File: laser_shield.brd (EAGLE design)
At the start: 114 x 85.1 mm, 18 parts, among them IC1 74AC08N, U1 ARDUINO_SHIELDLONGPADS

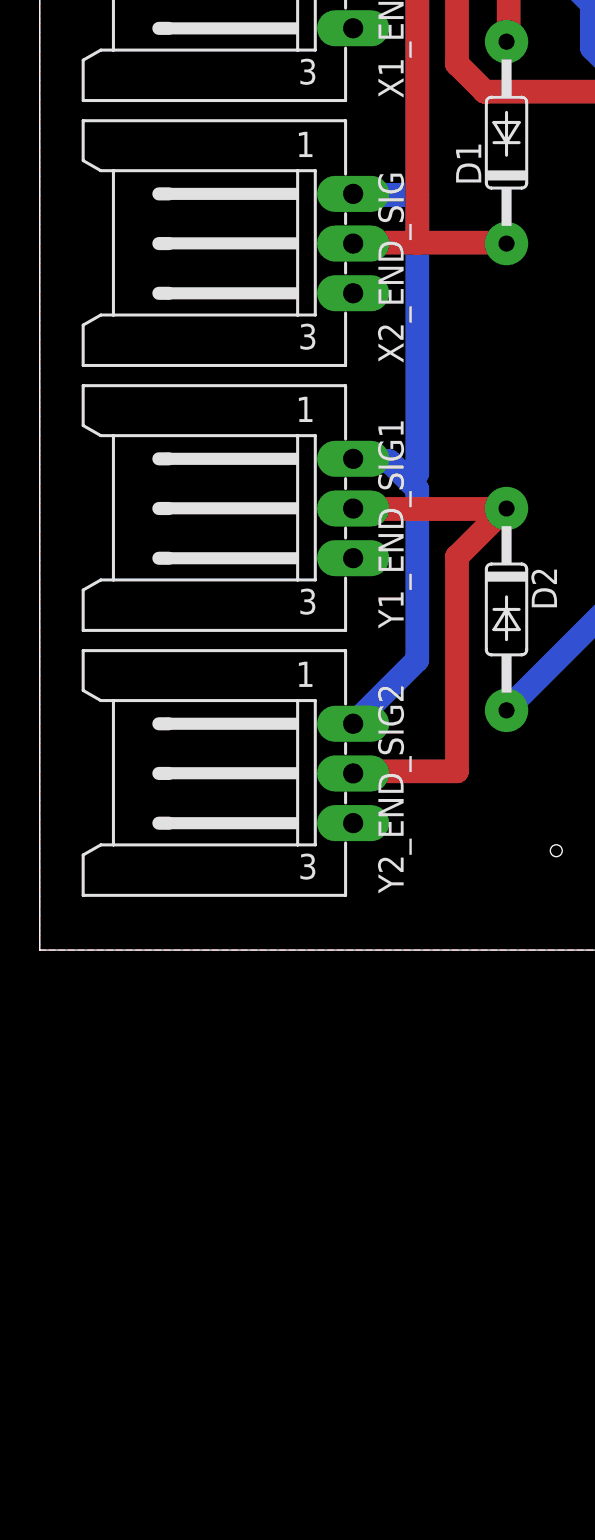
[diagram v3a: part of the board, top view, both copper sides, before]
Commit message: Added Z_LIMIT
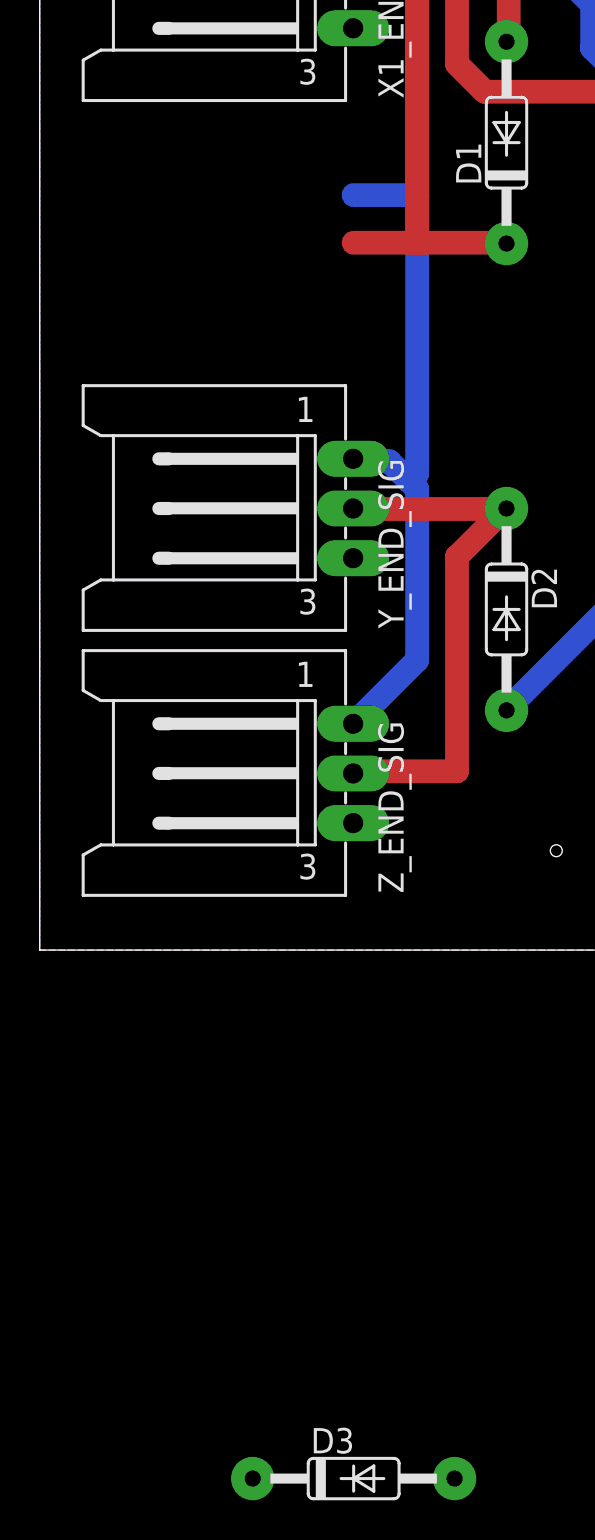
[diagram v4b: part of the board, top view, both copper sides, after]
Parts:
- removed X2_END_SIG: (no value), con-amp-mt:L03P
- added D3: 1N4148DO35-10, diode:DO35-10
- renumbered Y1_END_SIG1 to Y_END_SIG, Y2_END_SIG2 to Z_END_SIG
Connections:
- new net Z_END_STOP: D3.C, Z_END_SIG.2
- net GND: no longer X2_END_SIG.3
- net LIMIT_Z: now also D3.A
- net VCC_24: no longer X2_END_SIG.1
- net X_END_STOP: no longer X2_END_SIG.2
- net Y_END_STOP: no longer Z_END_SIG.2
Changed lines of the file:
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@@
 <attribute name="MF" value="" x="9.525" y="60.96" size="1.778" layer="27" rot="R90" display="off"/>
-</element>
-<element name="X2_END_SIG" library="con-amp-mt" package="L03P" value="" x="9.525" y="35.56" rot="R90">
-<attribute name="MPN" value="" x="9.525" y="35.56" size="1.778" layer="27" rot="R90" display="off"/>
-<attribute name="OC_NEWARK" value="unknown" x="9.525" y="35.56" size="1.778" layer="27" rot="R90" display="off"/>
-<attribute name="OC_FARNELL" value="unknown" x="9.525" y="35.56" size="1.778" layer="27" rot="R90" display="off"/>
-<attribute name="MF" value="" x="9.525" y="35.56" size="1.778" layer="27" rot="R90" display="off"/>
 </element>
 <element name="X1_END_SIG" library="con-amp-mt" package="L03P" value="" x="9.525" y="48.895" rot="R90">
@@
 <attribute name="MF" value="" x="127.635" y="29.21" size="1.778" layer="27" rot="R270" display="off"/>
 </element>
-<element name="Y1_END_SIG1" library="con-amp-mt" package="L03P" value="" x="9.525" y="22.225" rot="R90">
+<element name="Y_END_SIG" library="con-amp-mt" package="L03P" value="" x="9.525" y="22.225" rot="R90">
 <attribute name="MPN" value="" x="-12.065" y="1.27" size="1.778" layer="27" rot="R90" display="off"/>
 <attribute name="OC_NEWARK" value="unknown" x="-12.065" y="1.27" size="1.778" layer="27" rot="R90" display="off"/>
@@
 <attribute name="MF" value="" x="-12.065" y="1.27" size="1.778" layer="27" rot="R90" display="off"/>
 </element>
-<element name="Y2_END_SIG2" library="con-amp-mt" package="L03P" value="" x="9.525" y="8.89" rot="R90">
+<element name="Z_END_SIG" library="con-amp-mt" package="L03P" value="" x="9.525" y="8.89" rot="R90">
 <attribute name="MPN" value="" x="-12.065" y="-12.065" size="1.778" layer="27" rot="R90" display="off"/>
 <attribute name="OC_NEWARK" value="unknown" x="-12.065" y="-12.065" size="1.778" layer="27" rot="R90" display="off"/>
@@
 <attribute name="MF" value="" x="18.415" y="97.79" size="1.778" layer="27" display="off"/>
 </element>
+<element name="D3" library="diode" package="DO35-10" value="1N4148DO35-10" x="15.8" y="-26.6"/>
 </elements>
 <signals>
@@
 <contactref element="LASER_OUT" pad="1"/>
 <contactref element="RESET" pad="1"/>
-<contactref element="X2_END_SIG" pad="3"/>
 <contactref element="X1_END_SIG" pad="3"/>
 <contactref element="IC1" pad="7"/>
 <contactref element="PROBE" pad="1"/>
-<contactref element="Y1_END_SIG1" pad="3"/>
-<contactref element="Y2_END_SIG2" pad="3"/>
+<contactref element="Y_END_SIG" pad="3"/>
+<contactref element="Z_END_SIG" pad="3"/>
 <contactref element="MOTOR_Z" pad="1"/>
 <contactref element="FEED_H" pad="1"/>
@@
 <signal name="VCC_24" class="2">
 <contactref element="POWER_24V" pad="1"/>
-<contactref element="X2_END_SIG" pad="1"/>
 <contactref element="X1_END_SIG" pad="1"/>
-<contactref element="Y1_END_SIG1" pad="1"/>
-<contactref element="Y2_END_SIG2" pad="1"/>
+<contactref element="Y_END_SIG" pad="1"/>
+<contactref element="Z_END_SIG" pad="1"/>
 <wire x1="19" y1="14.6" x2="15.8" y2="11.4" width="1.2" layer="16"/>
 <wire x1="19" y1="23.2" x2="19" y2="14.6" width="1.2" layer="16"/>
@@
 <wire x1="19" y1="38" x2="15.8" y2="38" width="1.2" layer="16"/>
 <wire x1="19" y1="24" x2="19" y2="38" width="1.2" layer="16"/>
-<wire x1="15.8" y1="38" x2="15.775" y2="38.06" width="1.2" layer="16"/>
 <wire x1="19" y1="24" x2="18.6" y2="23.6" width="1.2" layer="16"/>
 <wire x1="19" y1="51.4" x2="15.8" y2="51.4" width="1.2" layer="16"/>
@@
 <signal name="LIMIT_Z">
 <contactref element="U1" pad="D12"/>
+<contactref element="D3" pad="A"/>
+<wire x1="20.88" y1="-26.6" x2="81.28" y2="22.86" width="0" layer="19" extent="1-1"/>
 </signal>
 <signal name="SPINDLE_DIR">
@@
 <signal name="Y_END_STOP">
 <contactref element="D2" pad="C"/>
-<contactref element="Y1_END_SIG1" pad="2"/>
-<contactref element="Y2_END_SIG2" pad="2"/>
+<contactref element="Y_END_SIG" pad="2"/>
 <wire x1="21" y1="9" x2="15.8" y2="9" width="1.2" layer="1"/>
 <wire x1="21" y1="19.8" x2="21" y2="9" width="1.2" layer="1"/>
 <wire x1="23.4" y1="22.2" x2="21" y2="19.8" width="1.2" layer="1"/>
-<wire x1="15.8" y1="9" x2="15.775" y2="8.89" width="1.2" layer="1"/>
 <wire x1="23.4" y1="22.2" x2="23.495" y2="22.225" width="1.2" layer="1"/>
 <wire x1="22.6" y1="22.2" x2="15.8" y2="22.2" width="1.2" layer="1"/>
@@
 <signal name="X_END_STOP">
 <contactref element="D1" pad="C"/>
-<contactref element="X2_END_SIG" pad="2"/>
 <contactref element="X1_END_SIG" pad="2"/>
 <wire x1="23.4" y1="35.6" x2="19" y2="35.6" width="1.2" layer="1"/>
 <wire x1="19" y1="35.6" x2="15.8" y2="35.6" width="1.2" layer="1"/>
-<wire x1="15.8" y1="35.6" x2="15.775" y2="35.56" width="1.2" layer="1"/>
 <wire x1="23.4" y1="35.6" x2="23.495" y2="35.56" width="1.2" layer="1"/>
 <wire x1="19" y1="48.8" x2="15.8" y2="48.8" width="1.2" layer="1"/>
@@
 <wire x1="33" y1="47" x2="33.02" y2="46.99" width="1.2" layer="16"/>
 </signal>
+<signal name="Z_END_STOP">
+<contactref element="Z_END_SIG" pad="2"/>
+<contactref element="D3" pad="C"/>
+<wire x1="10.72" y1="-26.6" x2="15.775" y2="8.89" width="0" layer="19" extent="1-1"/>
+</signal>
 </signals>
